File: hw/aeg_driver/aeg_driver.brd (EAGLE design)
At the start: 37 x 48 mm, 48 parts, among them J1 JST-ZH6SMT_VERT, J2 XT30XT30PW_MALE, U1 MAX150628TDFN, U2 TCAN334GSOT23, U3 STM32G474CEU6, U4 MC33926, U5 MC33926

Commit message: Checkpoint of aeg_driver
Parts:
- moved C11 7.64 mm to (22.9, 15.3), turned to 90 degrees
- moved U2 5.41 mm to (25.4, 15.3), turned to 270 degrees
- moved D1 1.58 mm to (8.50, 7.50)
- moved D2 1.58 mm to (10.5, 7.50)
- moved R3 1.58 mm to (8.50, 4.30)
- moved R4 1.58 mm to (10.5, 4.30)
- moved C7 1.23 mm to (1.90, 24.2)
- moved L1 1.16 mm to (4.80, 24.2)
- moved C8 1.15 mm to (9.30, 23.6)
- moved U1 1.09 mm to (8.40, 26.5)
- moved C9 1.05 mm to (10.9, 27.0)
- moved C12 1.03 mm to (18.4, 9.60)
- moved C13 1.02 mm to (17.2, 9.60)
- moved C14 1.01 mm to (16.0, 9.60)
- moved R1 1.00 mm to (20.9, 13.8), turned to 270 degrees
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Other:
- board text added: "aeg_driver r1 jjp@pobox.com (c) 2020"

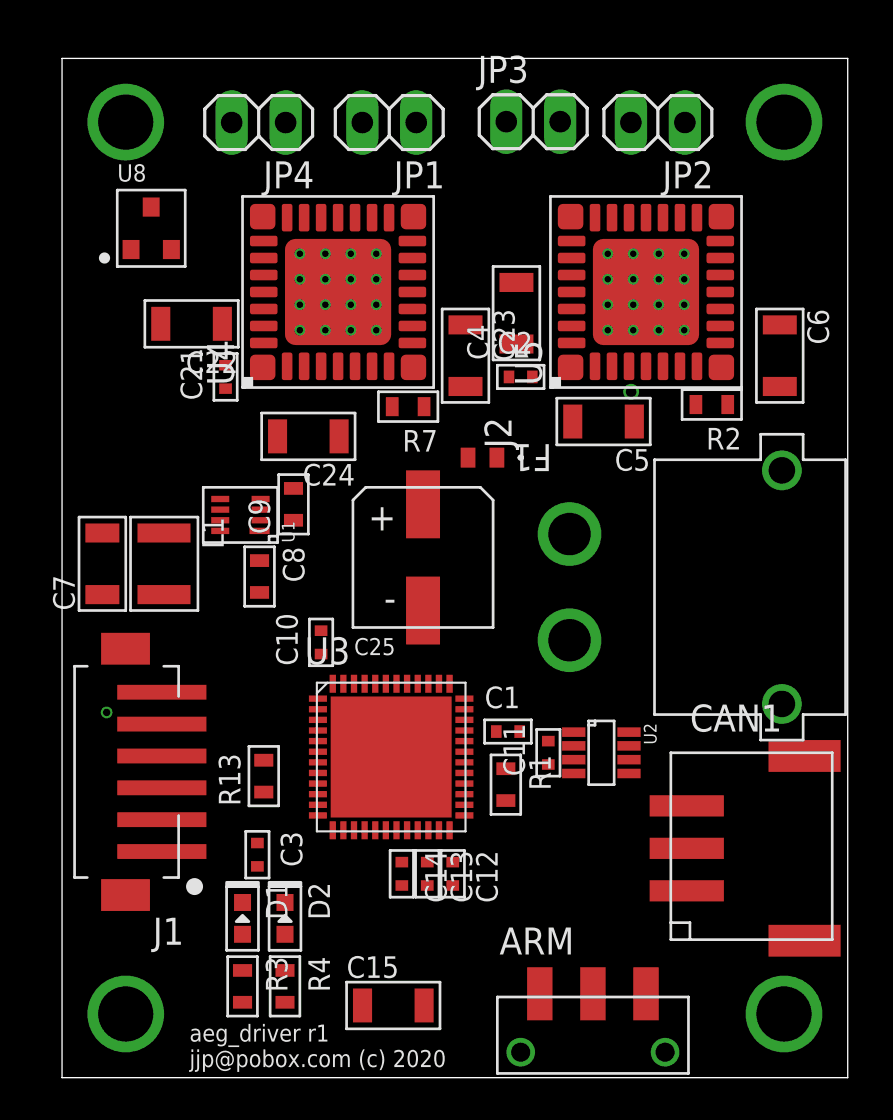
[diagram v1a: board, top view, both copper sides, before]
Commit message: aeg_driver: Route most power/gnd
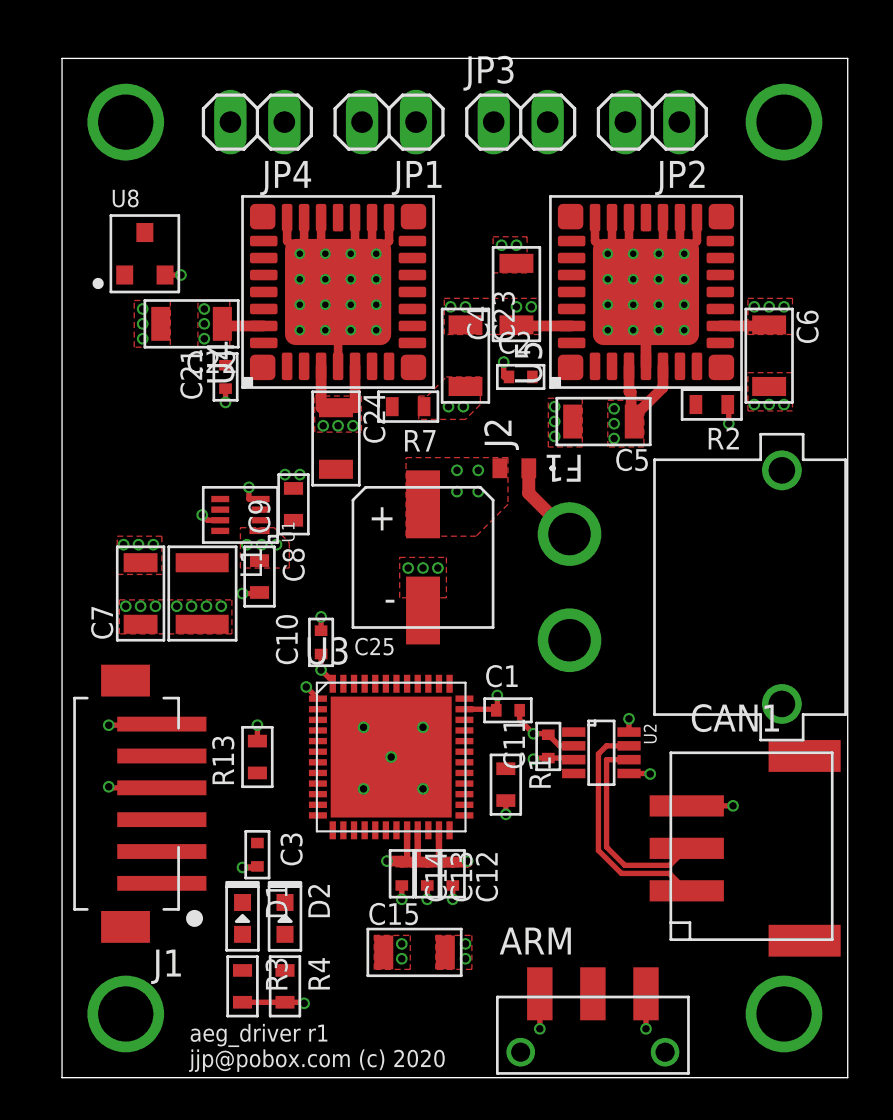
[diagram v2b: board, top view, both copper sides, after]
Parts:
- moved C15 2.69 mm to (16.6, 5.90)
- moved C7 2.28 mm to (3.70, 22.8)
- moved L1 2.28 mm to (6.60, 22.8)
- moved F1 1.58 mm to (21.3, 28.7)
- moved J1 1.50 mm to (2.70, 12.9)
- moved C24 1.30 mm to (12.9, 30.1), turned to 270 degrees
- moved U8 1.24 mm to (3.90, 38.8)
- moved C1 1.00 mm to (21.0, 17.3)
- moved R13 0.95 mm to (9.20, 15.1)
- moved C4 0.90 mm to (21.4, 36.9)
- moved JP3 0.59 mm to (21.6, 45.0)
- moved C6 0.50 mm to (33.3, 34.0)
- moved C11 0.30 mm to (22.9, 15.6)
- moved JP2 0.26 mm to (27.8, 45.0)
- moved JP4 0.06 mm to (9.20, 45.0)
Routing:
- net GND: track 0.00 -> 45.9 mm, vias 0 -> 43
- net VCC: track 0.00 -> 25.3 mm, vias 1 -> 21
- net V+: track 0.00 -> 20.1 mm, vias 1 -> 25
- net CAN_P: track 0.00 -> 11.1 mm
- net CAN_N: track 0.00 -> 9.64 mm
- net N$3: track 0.00 -> 3.90 mm
- added copper zone on layer 1, net GND
- added copper zone on layer 1, net V+
- added copper zone on layer 1, net VCC

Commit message: aeg_driver: Route drive, renumber, resize silks, rough silk place
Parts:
- removed C22, C23, C24: 10uF 50V, mfpassives:C1206
- removed C25: 100uF, aeg_driver:PANASONIC_FT_CAP_D
- removed JP1, JP4: (no value), pinhead:1X02
- removed R13: 18k, mfpassives:R0603
- removed R7: 560, mfpassives:R0603
- removed U8: (no value), mfdiscrete:SOT-23-3
- added C17, C18, C19: 10uF 50V, mfpassives:C1206
- added C20: 0.1uF 50V, mfpassives:C0402
- added J5: XT30XT30PW_MALE, controller:XT30PW_MALE
- added J6: JST-ZH6SMT_VERT, precharge:JST_B6B-ZR-SM4-TF(LF)(SN)
- added R5: 18k, mfpassives:R0603
- added R6: 560, mfpassives:R0603
- added U6: MC33926, gimbal:PQFN32
- C1: value 0.1uF -> 100uF; device mfpassives:C0402 -> aeg_driver:PANASONIC_FT_CAP_D
- C10: value 0.1uF -> 10uF 35V; device mfpassives:C0402 -> mfpassives:C1206
- C13: value 0.1uF -> 10uF 50V; device mfpassives:C0402 -> mfpassives:C1206
- C14: value 1uF -> 10uF 50V; device mfpassives:C0402 -> mfpassives:C1206
- C15: value 10uF 35V -> 10uF 50V
- C2: value 0.1uF 50V -> 1uF 50V; device mfpassives:C0402 -> mfpassives:C0603
- C3: value 0.1uF -> 1uF 50V; device mfpassives:C0402 -> mfpassives:C0603
- C4: value 10uF 50V -> 10uF 35V
- C5, C6: value 10uF 50V -> 0.1uF; device mfpassives:C1206 -> mfpassives:C0402
- C7: value 10uF 35V -> 1uF; device mfpassives:C1206 -> mfpassives:C0402
- C8, C9: value 1uF 50V -> 0.1uF; device mfpassives:C0603 -> mfpassives:C0402
- J1: value JST-ZH6SMT_VERT -> (none); device precharge:JST_B6B-ZR-SM4-TF(LF)(SN) -> pinhead:1X02
- J2: value XT30XT30PW_MALE -> (none); device controller:XT30PW_MALE -> pinhead:1X02
- R1: value 18k -> 220
- R2: value 560 -> 220
- R3: value 220 -> 18k
- R4: value 220 -> 560
- U1: value MAX150628TDFN -> (none); device precharge:8TDFN -> mfdiscrete:SOT-23-3
- U2: value TCAN334GSOT23 -> MAX150628TDFN; device controller:SOT23-8 -> precharge:8TDFN
- U4: value MC33926 -> TCAN334GSOT23; device gimbal:PQFN32 -> controller:SOT23-8
- moved R2 34.0 mm to (10.5, 4.30), turned to 270 degrees
- moved J1 32.8 mm to (9.20, 45.0), turned to 180 degrees
- moved C13 28.2 mm to (6.10, 35.5), turned to 180 degrees
- moved R4 27.9 mm to (16.3, 31.6), turned to 180 degrees
- moved C5 25.3 mm to (9.20, 11.5), turned to 270 degrees
- moved C6 25.0 mm to (12.2, 20.5), turned to 90 degrees
- moved U4 25.0 mm to (25.4, 15.3), turned to 270 degrees
- moved C14 24.6 mm to (19.0, 34.0)
- moved C15 24.5 mm to (12.9, 30.1), turned to 270 degrees
- moved J2 23.5 mm to (15.4, 45.0), turned to 180 degrees
- moved C4 22.6 mm to (3.70, 22.8)
- moved U2 20.4 mm to (8.40, 26.5), turned to 90 degrees
- moved C9 18.9 mm to (18.4, 9.60), turned to 270 degrees
- moved C7 18.0 mm to (16.0, 9.60), turned to 270 degrees
- moved C3 16.6 mm to (10.9, 27.0), turned to 90 degrees
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- renumbered C21 to C16, JP2 to J4, JP3 to J3
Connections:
- net AEG_D1: now also U6.26; no longer U5.26
- net AEG_FB: now also R6.P$2, U6.8; no longer R2.P$2, U5.8
- net AEG_OUT: now also U6.12, U6.13, U6.14, U6.15; no longer U5.12, U5.13, U5.14, U5.15
- net AEG_PWM: now also U6.2; no longer U5.2
- net AEG_SF: now also R5.P$1, U6.21; no longer R1.P$1, U5.21
- net CAN_N: now also U4.6; no longer U2.6
- net CAN_P: now also U4.7; no longer U2.7
- net CAN_RX: now also U4.4; no longer U2.4
- net CAN_TX: now also U4.1; no longer U2.1
- net GLOBAL_EN: now also U6.10; no longer U4.10
- net GND: now also C1.-, C17.P$2, C18.P$2, C19.P$2, C2.P$2, J5.2, J6.4, R4.P$1, R6.P$1, U1.P$2, U2.7, U4.2, U4.8, U6.18, U6.19, U6.20, U6.22, U6.23, U6.24, U6.5, U6.G0, U6.G1, U6.G10, U6.G11, U6.G12, U6.G13, U6.G14, U6.G15, U6.G16, U6.G2, U6.G3, U6.G4, U6.G5, U6.G6, U6.G7, U6.G8, U6.G9; no longer C1.P$2, C22.P$2, C23.P$2, C24.P$2, C25.-, J1.4, J2.2, R2.P$1, R7.P$1, U1.7, U2.2, U2.5, U2.8, U4.18, U4.19, U4.20, U4.22, U4.23, U4.24, U4.G0, U4.G1, U4.G10, U4.G11, U4.G12, U4.G13, U4.G14, U4.G15, U4.G16, U4.G2, U4.G3, U4.G4, U4.G5, U4.G6, U4.G7, U4.G8, U4.G9, U8.P$2
- net LASER_EN: now also U1.P$1; no longer U8.P$1
- net LOADER_D1: now also U5.26; no longer U4.26
- net LOADER_FB: now also R4.P$2, U5.8; no longer R7.P$2, U4.8
- net LOADER_OUT1: now also J2.1, U5.12, U5.13, U5.14, U5.15; no longer JP1.1, U4.12, U4.13, U4.14, U4.15
- net LOADER_OUT2: now also J2.2, U5.27, U5.28, U5.29, U5.30; no longer JP1.2, U4.27, U4.28, U4.29, U4.30
- net LOADER_PWM1: now also U5.2; no longer U4.2
- net LOADER_PWM2: now also U5.1; no longer U4.1
- net LOADER_SF: now also R3.P$1, U5.21; no longer R13.P$1, U4.21
- net LX: now also U2.8; no longer U1.8
- net MISC_OUT: now also U6.27, U6.28, U6.29, U6.30; no longer U5.27, U5.28, U5.29, U5.30
- net MISC_PWM: now also U6.1; no longer U5.1
- net N$1: now also C20.P$2, U6.32; no longer C2.P$2, U5.32
- net N$13: now also C3.P$1, U2.3; no longer C9.P$1, U1.3
- net N$2: now also J1.2, U1.P$3; no longer JP4.2, U8.P$3
- net N$3: now also J5.1; no longer J2.1
- net N$39: now also R1.P$1; no longer R3.P$1
- net N$40: now also R2.P$1; no longer R4.P$1
- net N$5: now also U5.32; no longer U4.32
- net NRST: now also C5.P$1, J6.2; no longer C3.P$1, J1.2
- net SWCLK: now also J6.5; no longer J1.5
- net SWDIO: now also J6.3; no longer J1.3
- net V+: now also C1.+, C13.P$1, C14.P$1, C15.P$1, C17.P$1, C18.P$1, C19.P$1, C20.P$1, U2.1, U2.2, U6.11, U6.31, U6.4, U6.6; no longer C22.P$1, C23.P$1, C24.P$1, C25.+, C4.P$1, C5.P$1, C6.P$1, C8.P$1, U1.1, U1.2, U4.11, U4.31, U4.4, U4.6
- net VCC: now also C4.P$1, C6.P$1, C8.P$1, C9.P$1, J1.1, J6.6, R2.P$2, R5.P$2, U2.4, U6.16, U6.3; no longer C1.P$1, C13.P$1, C14.P$1, C15.P$1, J1.6, JP4.1, R13.P$2, R4.P$2, U1.4, U2.3, U4.16
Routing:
- net LOADER_OUT2: track 0.00 -> 16.8 mm
- net AEG_OUT: track 0.00 -> 14.3 mm
- net LOADER_OUT1: track 0.00 -> 12.2 mm
- net MISC_OUT: track 0.00 -> 10.9 mm
- net GND: track 45.9 -> 48.9 mm, vias 43 -> 44
- net VCC: track 25.3 -> 27.5 mm, vias 21 -> 23
- added copper zone on layer 1, net AEG_OUT
- added copper zone on layer 1, net LOADER_OUT1
- added copper zone on layer 1, net LOADER_OUT2
- added copper zone on layer 1, net MISC_OUT

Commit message: aeg_driver: Draft autoroute
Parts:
- moved C14 0.20 mm to (18.8, 34.0)
- moved C17 0.20 mm to (21.2, 36.9)
- moved R4 0.20 mm to (16.1, 31.6)
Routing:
- net AEG_D1: track 0.00 -> 56.5 mm
- net SWDIO: track 0.00 -> 54.4 mm
- net GLOBAL_EN: track 0.00 -> 53.7 mm, vias 0 -> 3
- net AEG_SF: track 0.00 -> 42.5 mm, vias 0 -> 2
- net LASER_EN: track 0.00 -> 36.0 mm
- net LOADER_SF: track 0.00 -> 35.4 mm, vias 0 -> 2
- net LOADER_D1: track 0.00 -> 24.1 mm, vias 0 -> 2
- net AEG_FB: track 0.00 -> 23.6 mm, vias 0 -> 2
- net LOADER_FB: track 0.00 -> 23.5 mm, vias 0 -> 2
- net MISC_PWM: track 0.00 -> 21.7 mm
- net AEG_PWM: track 0.00 -> 20.7 mm
- net LOADER_PWM2: track 0.00 -> 18.6 mm
- net LOADER_PWM1: track 0.00 -> 18.5 mm, vias 0 -> 2
- net VCC: track 27.5 -> 45.7 mm, vias 23 -> 25
- net SWCLK: track 0.00 -> 16.0 mm, vias 0 -> 2
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
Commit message: aeg_driver: Curate BOM
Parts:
- C10, C4: value 10uF 35V -> 10uF 50V
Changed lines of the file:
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@@
 <element name="C11" library="mfpassives" package="C0402" value="0.1uF" x="21" y="17.3" smashed="yes">
 <attribute name="DIELECTRIC" value="" x="62.91" y="-30.96" size="1.778" layer="27" display="off"/>
-<attribute name="HOUSEPART" value="1" x="62.91" y="-30.96" size="1.778" layer="27" display="off"/>
+<attribute name="HOUSEPART" value="YES" x="62.91" y="-30.96" size="1.778" layer="27" display="off"/>
 <attribute name="MPN" value="MF-CAP-0402-0.1uF" x="62.91" y="-30.96" size="1.778" layer="27" display="off"/>
 <attribute name="NAME" x="21" y="18" size="0.8" layer="25" font="vector"/>
@@
 <element name="C6" library="mfpassives" package="C0402" value="0.1uF" x="12.2" y="20.5" smashed="yes" rot="R90">
 <attribute name="DIELECTRIC" value="" x="60.46" y="39.55" size="1.778" layer="27" rot="R90" display="off"/>
-<attribute name="HOUSEPART" value="1" x="60.46" y="39.55" size="1.778" layer="27" rot="R90" display="off"/>
+<attribute name="HOUSEPART" value="YES" x="60.46" y="39.55" size="1.778" layer="27" rot="R90" display="off"/>
 <attribute name="MPN" value="MF-CAP-0402-0.1uF" x="60.46" y="39.55" size="1.778" layer="27" rot="R90" display="off"/>
 <attribute name="NAME" x="11.5" y="20.6" size="0.8" layer="25" font="vector" rot="R180"/>
@@
 <element name="C9" library="mfpassives" package="C0402" value="0.1uF" x="18.4" y="9.6" smashed="yes" rot="R270">
 <attribute name="DIELECTRIC" value="" x="-29.86" y="-17.07" size="1.778" layer="27" rot="R270" display="off"/>
-<attribute name="HOUSEPART" value="1" x="-29.86" y="-17.07" size="1.778" layer="27" rot="R270" display="off"/>
+<attribute name="HOUSEPART" value="YES" x="-29.86" y="-17.07" size="1.778" layer="27" rot="R270" display="off"/>
 <attribute name="MPN" value="MF-CAP-0402-0.1uF" x="-29.86" y="-17.07" size="1.778" layer="27" rot="R270" display="off"/>
 <attribute name="NAME" x="19.2" y="8.6" size="0.8" layer="25" font="vector"/>
@@
 <element name="C8" library="mfpassives" package="C0402" value="0.1uF" x="17.2" y="9.6" smashed="yes" rot="R270">
 <attribute name="DIELECTRIC" value="" x="-31.06" y="-20.88" size="1.778" layer="27" rot="R270" display="off"/>
-<attribute name="HOUSEPART" value="1" x="-31.06" y="-20.88" size="1.778" layer="27" rot="R270" display="off"/>
+<attribute name="HOUSEPART" value="YES" x="-31.06" y="-20.88" size="1.778" layer="27" rot="R270" display="off"/>
 <attribute name="MPN" value="MF-CAP-0402-0.1uF" x="-31.06" y="-20.88" size="1.778" layer="27" rot="R270" display="off"/>
 <attribute name="NAME" x="16.7" y="7.3" size="0.8" layer="25" font="vector"/>
@@
 <element name="C7" library="mfpassives" package="C0402" value="1uF" x="16" y="9.6" smashed="yes" rot="R270">
 <attribute name="DIELECTRIC" value="" x="-32.26" y="-24.69" size="1.778" layer="27" rot="R270" display="off"/>
-<attribute name="HOUSEPART" value="1" x="-32.26" y="-24.69" size="1.778" layer="27" rot="R270" display="off"/>
+<attribute name="HOUSEPART" value="YES" x="-32.26" y="-24.69" size="1.778" layer="27" rot="R270" display="off"/>
 <attribute name="MPN" value="MF-CAP-0402-1uF" x="-32.26" y="-24.69" size="1.778" layer="27" rot="R270" display="off"/>
 <attribute name="NAME" x="15.2" y="9.4" size="0.8" layer="25" font="vector" rot="R180"/>
@@
 <attribute name="VOLTAGE" value="" x="-32.26" y="-24.69" size="1.778" layer="27" rot="R270" display="off"/>
 </element>
-<element name="C10" library="mfpassives" package="C1206" value="10uF 35V" x="16.6" y="5.9" smashed="yes">
+<element name="C10" library="mfpassives" package="C1206" value="10uF 50V" x="16.6" y="5.9" smashed="yes">
 <attribute name="DIELECTRIC" value="" x="36.92" y="-38.55" size="1.778" layer="27" display="off"/>
 <attribute name="HOUSEPART" value="" x="36.92" y="-38.55" size="1.778" layer="27" display="off"/>
 <attribute name="MF" value="TDK" x="36.92" y="-38.55" size="1.778" layer="27" display="off"/>
-<attribute name="MPN" value="CGA5L1X7R1V106K160AC" x="36.92" y="-38.55" size="1.778" layer="27" display="off"/>
+<attribute name="MPN" value="C3216X7R1H106K160AE" x="36.92" y="-38.55" size="1.778" layer="27" display="off"/>
 <attribute name="NAME" x="17.6" y="4.6" size="0.8" layer="25" font="vector" rot="R180"/>
 <attribute name="POPULATE" value="1" x="36.92" y="-38.55" size="1.778" layer="27" display="off"/>
@@
 <element name="C5" library="mfpassives" package="C0402" value="0.1uF" x="9.2" y="11.5" smashed="yes" rot="R270">
 <attribute name="DIELECTRIC" value="" x="-39.06" y="-38.03" size="1.778" layer="27" rot="R270" display="off"/>
-<attribute name="HOUSEPART" value="1" x="-39.06" y="-38.03" size="1.778" layer="27" rot="R270" display="off"/>
+<attribute name="HOUSEPART" value="YES" x="-39.06" y="-38.03" size="1.778" layer="27" rot="R270" display="off"/>
 <attribute name="MPN" value="MF-CAP-0402-0.1uF" x="-39.06" y="-38.03" size="1.778" layer="27" rot="R270" display="off"/>
 <attribute name="NAME" x="9.9" y="11.8" size="0.8" layer="25" font="vector"/>
@@
 <attribute name="VOLTAGE" value="" x="-4.8" y="-18.07" size="1.778" layer="27" rot="R270" display="off"/>
 </element>
-<element name="C4" library="mfpassives" package="C1206" value="10uF 35V" x="3.7" y="22.8" smashed="yes" rot="R90">
+<element name="C4" library="mfpassives" package="C1206" value="10uF 50V" x="3.7" y="22.8" smashed="yes" rot="R90">
 <attribute name="DIELECTRIC" value="" x="48.15" y="38.04" size="1.778" layer="27" rot="R90" display="off"/>
 <attribute name="HOUSEPART" value="" x="48.15" y="38.04" size="1.778" layer="27" rot="R90" display="off"/>
 <attribute name="MF" value="TDK" x="48.15" y="38.04" size="1.778" layer="27" rot="R90" display="off"/>
-<attribute name="MPN" value="CGA5L1X7R1V106K160AC" x="48.15" y="38.04" size="1.778" layer="27" rot="R90" display="off"/>
+<attribute name="MPN" value="C3216X7R1H106K160AE" x="48.15" y="38.04" size="1.778" layer="27" rot="R90" display="off"/>
 <attribute name="NAME" x="2.6" y="25.6" size="0.8" layer="25" font="vector"/>
 <attribute name="POPULATE" value="1" x="48.15" y="38.04" size="1.778" layer="27" rot="R90" display="off"/>
@@
 </element>
 <element name="J5" library="controller" package="XT30PW_MALE" value="XT30XT30PW_MALE" x="23.9" y="23.1" smashed="yes" rot="R270">
+<attribute name="MPN" value="XT30PW-M" x="23.9" y="23.1" size="1.778" layer="27" rot="R270" display="off"/>
 <attribute name="NAME" x="36.5" y="30.1" size="1" layer="25" rot="R90"/>
-<attribute name="POPULATE" value="0" x="18.82" y="-15" size="1.778" layer="27" rot="R270" display="off"/>
+<attribute name="POPULATE" value="1" x="18.82" y="-15" size="1.778" layer="27" rot="R270" display="off"/>
 </element>
 <element name="J2" library="pinhead" library_urn="urn:adsk.eagle:library:325" package="1X02" package3d_urn="urn:adsk.eagle:package:22435/2" value="" x="15.4" y="45" smashed="yes" rot="R180">
 <attribute name="NAME" x="14.7838" y="46.6288" size="1" layer="25"/>
 <attribute name="POPULARITY" value="98" x="-1.11" y="78.02" size="1.778" layer="27" rot="R180" display="off"/>
+<attribute name="POPULATE" value="0" x="15.4" y="45" size="1.778" layer="27" rot="R180" display="off"/>
 <attribute name="VALUE" x="17.94" y="48.175" size="1.27" layer="27" rot="R180"/>
 </element>
@@
 <attribute name="NAME" x="27.1838" y="46.5288" size="1" layer="25"/>
 <attribute name="POPULARITY" value="98" x="4.94" y="78.02" size="1.778" layer="27" rot="R180" display="off"/>
+<attribute name="POPULATE" value="0" x="27.8" y="45" size="1.778" layer="27" rot="R180" display="off"/>
 <attribute name="VALUE" x="30.34" y="48.175" size="1.27" layer="27" rot="R180"/>
 </element>
@@
 <attribute name="NAME" x="21.0838" y="46.5288" size="1" layer="25"/>
 <attribute name="POPULARITY" value="98" x="50.81" y="11.98" size="1.778" layer="27" display="off"/>
+<attribute name="POPULATE" value="0" x="21.6" y="45" size="1.778" layer="27" display="off"/>
 <attribute name="VALUE" x="19.06" y="41.825" size="1.27" layer="27"/>
 </element>
@@
 <attribute name="NAME" x="8.6838" y="46.6288" size="1" layer="25"/>
 <attribute name="POPULARITY" value="98" x="-26.36" y="78.02" size="1.778" layer="27" rot="R180" display="off"/>
+<attribute name="POPULATE" value="0" x="9.2" y="45" size="1.778" layer="27" rot="R180" display="off"/>
 <attribute name="VALUE" x="11.74" y="48.175" size="1.27" layer="27" rot="R180"/>
 </element>
